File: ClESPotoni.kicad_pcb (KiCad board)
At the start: 2 copper layers, 55.2 x 60.4 mm, 47 parts, among them J1 Conn_01x06, Q1 Q_NMOS_GSD, Q2 Q_NMOS_GSD, Q3 BC817, SW1 Flash, SW2 RESET, U1 ESP32-WROOM-32, U2 DRV8833PW, U3 LD1117S33TR_SOT223

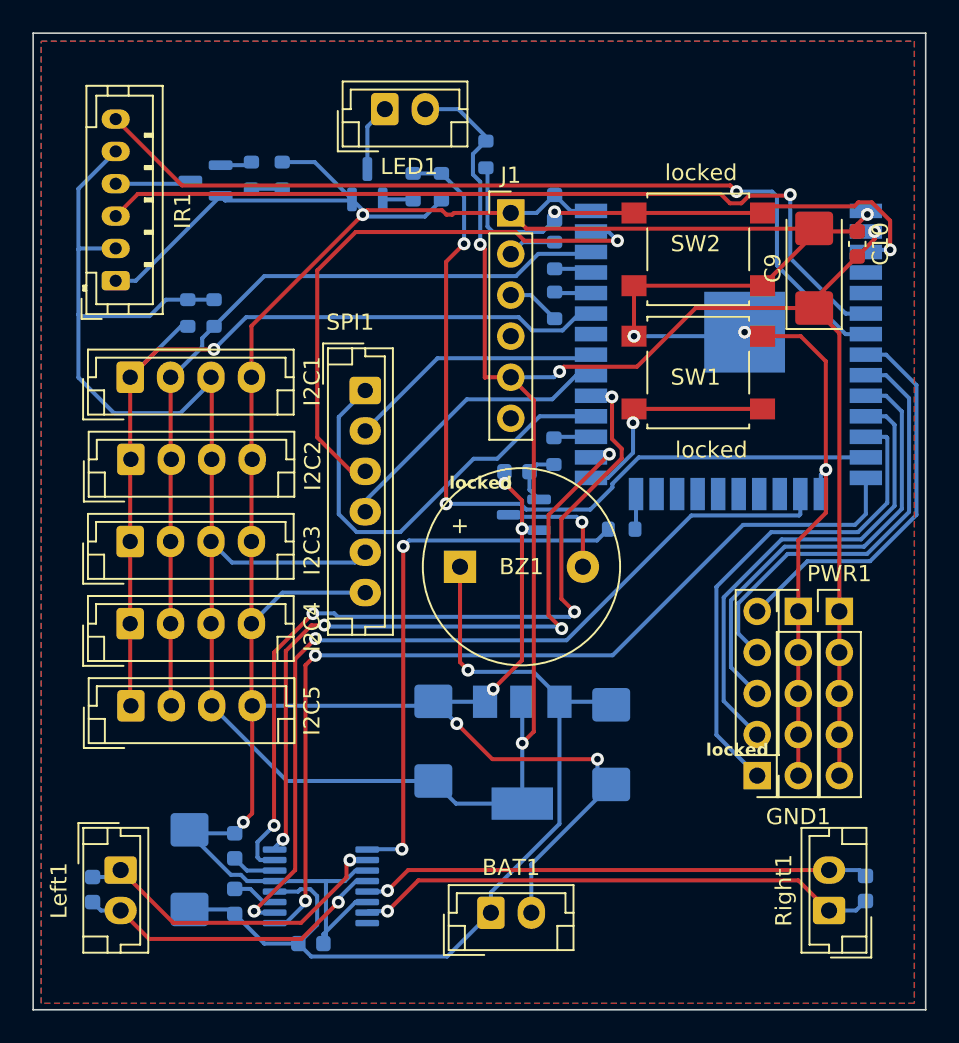
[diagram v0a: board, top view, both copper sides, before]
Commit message: New version for ESP32-S3-WROOM-1, with bugfixes
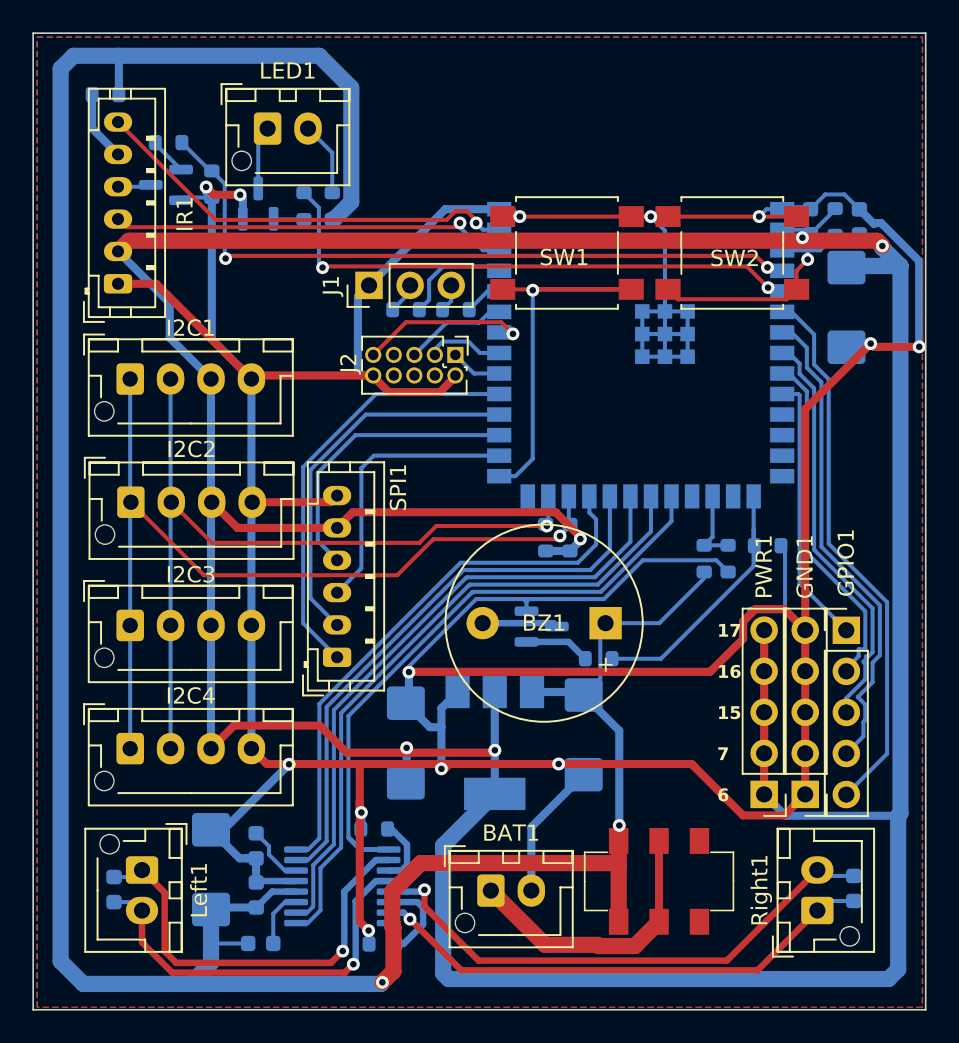
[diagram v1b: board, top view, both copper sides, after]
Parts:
- removed C12: C, Capacitor_SMD:C_0603_1608Metric
- removed I2C5: Conn_01x04_Male, Connector_JST:JST_EH_B4B-EH-A_1x04_P2.50mm_Vertical
- added J2: AVR-JTAG-10, Connector_PinHeader_1.27mm:PinHeader_2x05_P1.27mm_Vertical, F.Cu at (126.1, 79.9)
- added R12: 0.2R, Resistor_SMD:R_0603_1608Metric, B.Cu at (121.1, 109.2)
- added R13: 0.2R, Resistor_SMD:R_0603_1608Metric, B.Cu at (121.6, 116.3)
- added R14: 10K, Resistor_SMD:R_0603_1608Metric, B.Cu at (143.0, 92.5)
- added R15: 10k, Resistor_SMD:R_0603_1608Metric, B.Cu at (141.5, 92.5)
- added R16: 10K, Resistor_SMD:R_0603_1608Metric, B.Cu at (145.4, 91.7)
- added SW3: SW_DPDT_x2, Switch_DPDT:Switch_DPDT, F.Cu at (138.7, 112.5)
- BAT1, LED1, Left1, Right1: footprint Connector_JST:JST_EH_B2B-EH-A_1x02_P2.50mm_Vertical -> Connector_JST:JST_XH_B2B-XH-AM_1x02_P2.50mm_Vertical
- C10, C9: moved to B.Cu
- C11: value 100n -> 1u
- C7, C8: value C_Polarized -> 10u
- GND1, GPIO1, PWR1: value Conn_01x05_Male -> Conn_01x04_Male
- I2C1, I2C2, I2C3, I2C4: footprint Connector_JST:JST_EH_B4B-EH-A_1x04_P2.50mm_Vertical -> Connector_JST:JST_XH_B4B-XH-AM_1x04_P2.50mm_Vertical
- J1: footprint Connector_PinHeader_2.54mm:PinHeader_1x06_P2.54mm_Vertical -> Connector_PinHeader_2.54mm:PinHeader_1x03_P2.54mm_Vertical
- R11: value R -> 330
- R2: value 10k -> 330R
- R3: value 10k -> ?R
- SPI1: footprint Connector_JST:JST_EH_B6B-EH-A_1x06_P2.50mm_Vertical -> Connector_JST:JST_PH_B6B-PH-K_1x06_P2.00mm_Vertical
- U1: value ESP32-WROOM-32 -> ESP32-S3-WROOM-1; footprint RF_Module:ESP32-WROOM-32 -> Espressif:ESP32-S3-WROOM-1
- moved R3 41.7 mm to (104.5, 63.8)
- moved R4 27.4 mm to (133.2, 91.2), turned to -90 degrees
- moved R5 24.8 mm to (131.7, 91.2), turned to -90 degrees
- moved R10 22.0 mm to (149.6, 71.7)
- moved C11 18.9 mm to (151.1, 71.7)
- moved SPI1 16.6 mm to (118.8, 98.6), turned to 90 degrees
- moved R11 13.1 mm to (135.0, 98.7), turned to 180 degrees
- moved PWR1 12.2 mm to (145.2, 107.1), turned to 180 degrees
- moved GND1 11.3 mm to (147.8, 107.1), turned to 180 degrees
- moved SW1 11.0 mm to (133.0, 73.6)
- moved GPIO1 10.5 mm to (150.3, 96.9), turned to 0 degrees
- moved J1 9.84 mm to (120.8, 75.6), turned to 90 degrees
- moved R8 9.78 mm to (123.1, 77.1), turned to 0 degrees
- moved BZ1 9.65 mm to (135.4, 96.5), turned to 180 degrees
- moved I2C4 7.73 mm to (106.0, 104.2)
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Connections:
- BAT1 pad 1: +BATT -> Net-(BAT1-+)
- GPIO1 pad 1: /IO27 -> /IO17
- GPIO1 pad 2: /IO26 -> /IO16
- GPIO1 pad 3: /IO25 -> /IO15
- GPIO1 pad 4: /IO33 -> /IO07
- GPIO1 pad 5: /IO32 -> /IO06
- IR1 pad 5: +3.3V -> /IRLED+/A1
- LED1 pad 2: +3.3V -> Net-(LED1-Pin_2)
- R2 pad 1: GND -> +BATT
- R2 pad 2: /HEADLED -> Net-(LED1-Pin_2)
- R3 pad 1: Net-(U1-IO2) -> +BATT
- R3 pad 2: /M_sleep -> /IRLED+/A1
- SW1 pad 1: Net-(U1-IO0) -> /BOOT
- U1 pad 10: /IO25 -> /IO17
- U1 pad 11: /IO26 -> unconnected-(U1-GPIO18/U1RXD/ADC2_CH7/CLK_OUT3-Pad11)
- U1 pad 12: /IO27 -> unconnected-(U1-GPIO8/TOUCH8/ADC1_CH7/SUBSPICS1-Pad12)
- U1 pad 13: /HEADLED -> unconnected-(U1-GPIO19/U1RTS/ADC2_CH8/CLK_OUT2/USB_D--Pad13)
- U1 pad 14: /BIN1 -> unconnected-(U1-GPIO20/U1CTS/ADC2_CH9/CLK_OUT1/USB_D+-Pad14)
- U1 pad 15: GND -> /BUZZ
- U1 pad 16: /BIN2 -> unconnected-(U1-GPIO46-Pad16)
- U1 pad 17: unconnected-(U1-SHD/SD2-Pad17) -> /BAT_SENSE
- U1 pad 19: unconnected-(U1-SCS/CMD-Pad19) -> /M_sleep
- U1 pad 20: unconnected-(U1-SCK/CLK-Pad20) -> /BIN1
- U1 pad 21: unconnected-(U1-SDO/SD0-Pad21) -> /BIN2
- U1 pad 22: unconnected-(U1-SDI/SD1-Pad22) -> /AIN2
- U1 pad 23: unconnected-(U1-IO15-Pad23) -> /AIN1
- U1 pad 24: Net-(U1-IO2) -> /SDA
- U1 pad 25: Net-(U1-IO0) -> /SCL
- U1 pad 26: /AIN1 -> unconnected-(U1-GPIO45-Pad26)
- U1 pad 27: /BUZZ -> /BOOT
- U1 pad 28: /CS -> /MOSI
- U1 pad 29: /AIN2 -> /CLK
- U1 pad 30: /CLK -> /MISO
- U1 pad 31: /MISO -> /CS
- U1 pad 32: unconnected-(U1-NC-Pad32) -> /TCK
- U1 pad 33: /SDA -> /TDO
- U1 pad 34: /RXD -> /TDI
- U1 pad 35: /TXD -> /TMS
- U1 pad 36: /SCL -> /RXD
- U1 pad 37: /MOSI -> /TXD
- U1 pad 38: GND -> /A4/SL
- U1 pad 39: GND -> /A8/SR
- U1 pad 4: unconnected-(U1-SENSOR_VP-Pad4) -> /IRLED
- U1 pad 5: unconnected-(U1-SENSOR_VN-Pad5) -> /HEADLED
- U1 pad 6: /A4/SL -> /IO06
- U1 pad 7: /A8/SR -> /IO07
- U1 pad 8: /IO32 -> /IO15
- U1 pad 9: /IO33 -> /IO16
- U2 pad 3: GND -> Net-(U2-AISEN)
- U2 pad 6: GND -> Net-(U2-BISEN)
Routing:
- net +BATT: track 58.6 -> 174.5 mm, vias 1 -> 2
- net GND: track 250.9 -> 325.2 mm, vias 11 -> 13
- net +3.3V: track 196.7 -> 251.0 mm, vias 4 -> 5
- net /IRLED: track 1.91 -> 43.1 mm, vias 0 -> 2
- net /IO06: track 0.00 -> 33.3 mm
- net /IO27: track 30.8 -> 0.00 mm
- net /IO07: track 0.00 -> 29.5 mm
- net /IO26: track 29.3 -> 0.00 mm
- net /A4/SL: track 52.8 -> 24.7 mm
- net /IO25: track 28.0 -> 0.00 mm
- net /A8/SR: track 54.4 -> 26.9 mm
- net /BOOT: track 0.00 -> 27.0 mm, vias 0 -> 1
- net /IO33: track 26.7 -> 0.00 mm
- net /IO15: track 0.00 -> 25.2 mm
- net /IO32: track 24.3 -> 0.00 mm
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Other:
- board text added: "17 16 15 7 6"
- board text removed: "locked"
